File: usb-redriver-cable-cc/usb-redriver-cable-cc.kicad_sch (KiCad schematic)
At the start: 33 parts, among them J1 USB3 IN, J2 USB3 OUT, U1 PTN36241BBS, U2 SE8119AKN

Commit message: Transcribe strapping resistors with interpretations
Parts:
- R1, R10, R4, R7: value R -> 0
- R11, R13, R14, R2, R3, R5, R8, R9: value R -> DNP
- R12: value R -> 44k5
- R6: value R -> 38k
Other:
- note added: "Channel A & B Input signal threshold: 75 mV"
- note added: "Channel A Receive equalization: 7.5 dB Transmit de-emphasis: 0 dB Output swing: 1100 mV"
- note added: "Channel B Receive equalization: 7.5 dB Transmit de-emphasis: 0 dB Output swing: 1100 mV"
- moved on the sheet: C11, C12, C13, C14, C15, R1, R10, R2, R3, R4, R5, R6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

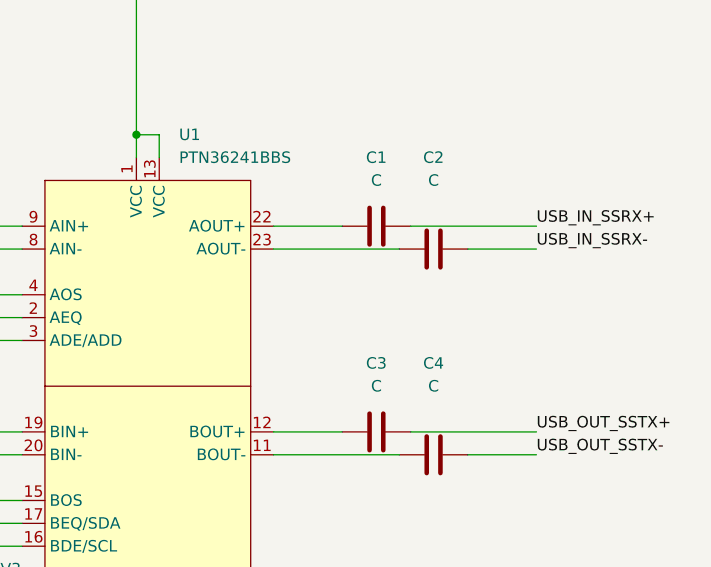
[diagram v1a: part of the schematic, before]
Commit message: Values for AC coupling capacitors
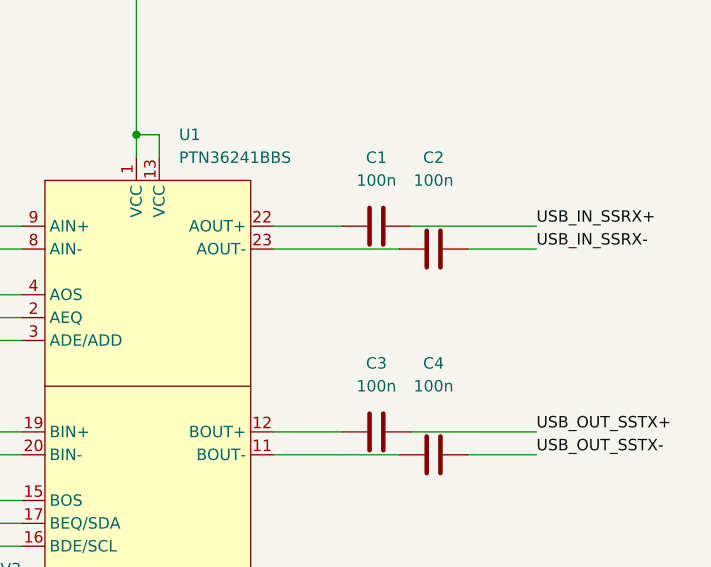
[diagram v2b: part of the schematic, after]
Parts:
- C1, C2, C3, C4: value C -> 100n
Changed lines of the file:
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@@
 			)
 		)
-		(property "Value" "C"
+		(property "Value" "100n"
 			(at 238.76 64.77 90)
 			(effects
@@
 			)
 		)
-		(property "Value" "C"
+		(property "Value" "100n"
 			(at 232.41 64.77 90)
 			(effects
@@
 			)
 		)
-		(property "Value" "C"
+		(property "Value" "100n"
 			(at 238.76 87.63 90)
 			(effects
@@
 			)
 		)
-		(property "Value" "C"
+		(property "Value" "100n"
 			(at 232.41 87.63 90)
 			(effects

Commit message: Footprint for AC coupling capacitors
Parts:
- C1, C2, C3, C4: footprint (none) -> Capacitor_SMD:C_0402_1005Metric
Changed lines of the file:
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@@
 			)
 		)
-		(property "Footprint" ""
+		(property "Footprint" "Capacitor_SMD:C_0402_1005Metric"
 			(at 242.57 71.4248 0)
 			(effects
@@
 			)
 		)
-		(property "Footprint" ""
+		(property "Footprint" "Capacitor_SMD:C_0402_1005Metric"
 			(at 236.22 68.8848 0)
 			(effects
@@
 			)
 		)
-		(property "Footprint" ""
+		(property "Footprint" "Capacitor_SMD:C_0402_1005Metric"
 			(at 242.57 94.2848 0)
 			(effects
@@
 			)
 		)
-		(property "Footprint" ""
+		(property "Footprint" "Capacitor_SMD:C_0402_1005Metric"
 			(at 236.22 91.7448 0)
 			(effects

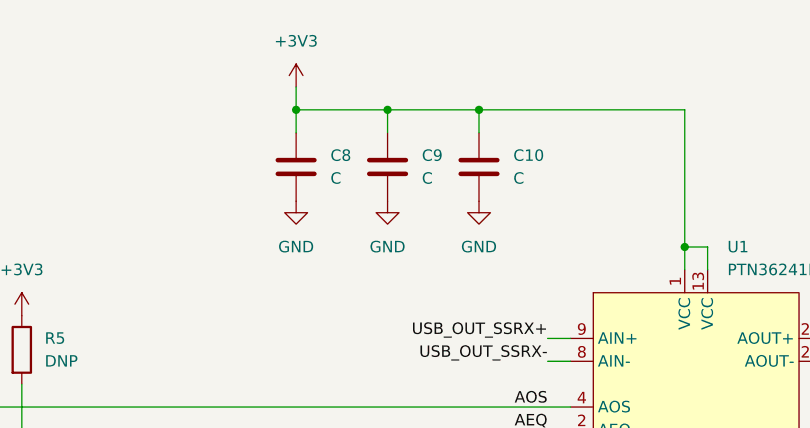
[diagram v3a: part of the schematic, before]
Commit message: Add values for redriver decoupling capacitors
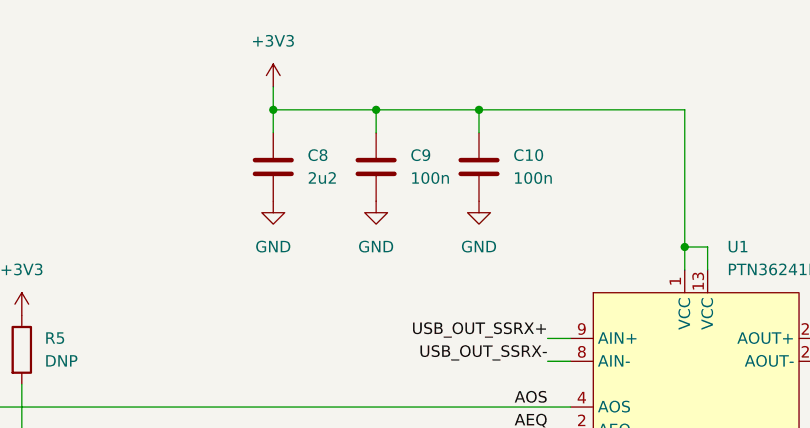
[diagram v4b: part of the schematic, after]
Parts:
- C10, C9: value C -> 100n; footprint (none) -> Capacitor_SMD:C_0402_1005Metric
- C8: value C -> 2u2; footprint (none) -> Capacitor_SMD:C_0805_2012Metric
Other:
- moved on the sheet: C8, C9
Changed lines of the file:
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@@
 	)
 	(junction
-		(at 162.56 44.45)
+		(at 160.02 44.45)
 		(diameter 0)
 		(color 0 0 0 0)
@@
 	)
 	(junction
-		(at 172.72 44.45)
+		(at 171.45 44.45)
 		(diameter 0)
 		(color 0 0 0 0)
@@
 	(wire
 		(pts
-			(xy 162.56 44.45) (xy 172.72 44.45)
+			(xy 160.02 44.45) (xy 171.45 44.45)
 		)
 		(stroke
@@
 	(wire
 		(pts
-			(xy 162.56 46.99) (xy 162.56 44.45)
+			(xy 160.02 46.99) (xy 160.02 44.45)
 		)
 		(stroke
@@
 	(wire
 		(pts
-			(xy 172.72 44.45) (xy 182.88 44.45)
+			(xy 171.45 44.45) (xy 182.88 44.45)
 		)
 		(stroke
@@
 	(wire
 		(pts
-			(xy 172.72 44.45) (xy 172.72 46.99)
+			(xy 171.45 44.45) (xy 171.45 46.99)
 		)
 		(stroke
@@
 	(wire
 		(pts
-			(xy 162.56 41.91) (xy 162.56 44.45)
+			(xy 160.02 41.91) (xy 160.02 44.45)
 		)
 		(stroke
@@
 	(symbol
 		(lib_id "Device:C")
-		(at 172.72 50.8 0)
+		(at 171.45 50.8 0)
 		(unit 1)
 		(exclude_from_sim no)
@@
 		(fields_autoplaced yes)
 		(property "Reference" "C9"
-			(at 176.53 49.5299 0)
+			(at 175.26 49.5299 0)
 			(effects
 				(font
@@
 			)
 		)
-		(property "Value" "C"
-			(at 176.53 52.0699 0)
+		(property "Value" "100n"
+			(at 175.26 52.0699 0)
 			(effects
 				(font
@@
 			)
 		)
-		(property "Footprint" ""
-			(at 173.6852 54.61 0)
+		(property "Footprint" "Capacitor_SMD:C_0402_1005Metric"
+			(at 172.4152 54.61 0)
 			(effects
 				(font
@@
 		)
 		(property "Datasheet" "~"
-			(at 172.72 50.8 0)
+			(at 171.45 50.8 0)
 			(effects
 				(font
@@
 		)
 		(property "Description" "Unpolarized capacitor"
-			(at 172.72 50.8 0)
+			(at 171.45 50.8 0)
 			(effects
 				(font
@@
 	(symbol
 		(lib_id "power:GND")
-		(at 162.56 54.61 0)
+		(at 160.02 54.61 0)
 		(unit 1)
 		(exclude_from_sim no)
@@
 		(fields_autoplaced yes)
 		(property "Reference" "#PWR024"
-			(at 162.56 60.96 0)
+			(at 160.02 60.96 0)
 			(effects
 				(font
@@
 		)
 		(property "Value" "GND"
-			(at 162.56 59.69 0)
+			(at 160.02 59.69 0)
 			(effects
 				(font
@@
 		)
 		(property "Footprint" ""
-			(at 162.56 54.61 0)
+			(at 160.02 54.61 0)
 			(effects
 				(font
@@
 		)
 		(property "Datasheet" ""
-			(at 162.56 54.61 0)
+			(at 160.02 54.61 0)
 			(effects
 				(font
@@
 		)
 		(property "Description" "Power symbol creates a global label with name \"GND\" , ground"
-			(at 162.56 54.61 0)
+			(at 160.02 54.61 0)
 			(effects
 				(font
@@
 	(symbol
 		(lib_id "power:+3V3")
-		(at 162.56 41.91 0)
+		(at 160.02 41.91 0)
 		(unit 1)
 		(exclude_from_sim no)
@@
 		(fields_autoplaced yes)
 		(property "Reference" "#PWR018"
-			(at 162.56 45.72 0)
+			(at 160.02 45.72 0)
 			(effects
 				(font
@@
 		)
 		(property "Value" "+3V3"
-			(at 162.56 36.83 0)
+			(at 160.02 36.83 0)
 			(effects
 				(font
@@
 		)
 		(property "Footprint" ""
-			(at 162.56 41.91 0)
+			(at 160.02 41.91 0)
 			(effects
 				(font
@@
 		)
 		(property "Datasheet" ""
-			(at 162.56 41.91 0)
+			(at 160.02 41.91 0)
 			(effects
 				(font
@@
 		)
 		(property "Description" "Power symbol creates a global label with name \"+3V3\""
-			(at 162.56 41.91 0)
+			(at 160.02 41.91 0)
 			(effects
 				(font
@@
 			)
 		)
-		(property "Value" "C"
+		(property "Value" "100n"
 			(at 186.69 52.0699 0)
 			(effects
@@
 			)
 		)
-		(property "Footprint" ""
+		(property "Footprint" "Capacitor_SMD:C_0402_1005Metric"
 			(at 183.8452 54.61 0)
 			(effects
@@
 	(symbol
 		(lib_id "power:GND")
-		(at 172.72 54.61 0)
+		(at 171.45 54.61 0)
 		(unit 1)
 		(exclude_from_sim no)
@@
 		(fields_autoplaced yes)
 		(property "Reference" "#PWR025"
-			(at 172.72 60.96 0)
+			(at 171.45 60.96 0)
 			(effects
 				(font
@@
 		)
 		(property "Value" "GND"
-			(at 172.72 59.69 0)
+			(at 171.45 59.69 0)
 			(effects
 				(font
@@
 		)
 		(property "Footprint" ""
-			(at 172.72 54.61 0)
+			(at 171.45 54.61 0)
 			(effects
 				(font
@@
 		)
 		(property "Datasheet" ""
-			(at 172.72 54.61 0)
+			(at 171.45 54.61 0)
 			(effects
 				(font
@@
 		)
 		(property "Description" "Power symbol creates a global label with name \"GND\" , ground"
-			(at 172.72 54.61 0)
+			(at 171.45 54.61 0)
 			(effects
 				(font
@@
 	(symbol
 		(lib_id "Device:C")
-		(at 162.56 50.8 0)
+		(at 160.02 50.8 0)
 		(unit 1)
 		(exclude_from_sim no)
@@
 		(fields_autoplaced yes)
 		(property "Reference" "C8"
-			(at 166.37 49.5299 0)
+			(at 163.83 49.5299 0)
 			(effects
 				(font
@@
 			)
 		)
-		(property "Value" "C"
-			(at 166.37 52.0699 0)
+		(property "Value" "2u2"
+			(at 163.83 52.0699 0)
 			(effects
 				(font
@@
 			)
 		)
-		(property "Footprint" ""
-			(at 163.5252 54.61 0)
+		(property "Footprint" "Capacitor_SMD:C_0805_2012Metric"
+			(at 160.9852 54.61 0)
 			(effects
 				(font
@@
 		)
 		(property "Datasheet" "~"
-			(at 162.56 50.8 0)
+			(at 160.02 50.8 0)
 			(effects
 				(font
@@
 		)
 		(property "Description" "Unpolarized capacitor"
-			(at 162.56 50.8 0)
+			(at 160.02 50.8 0)
 			(effects
 				(font

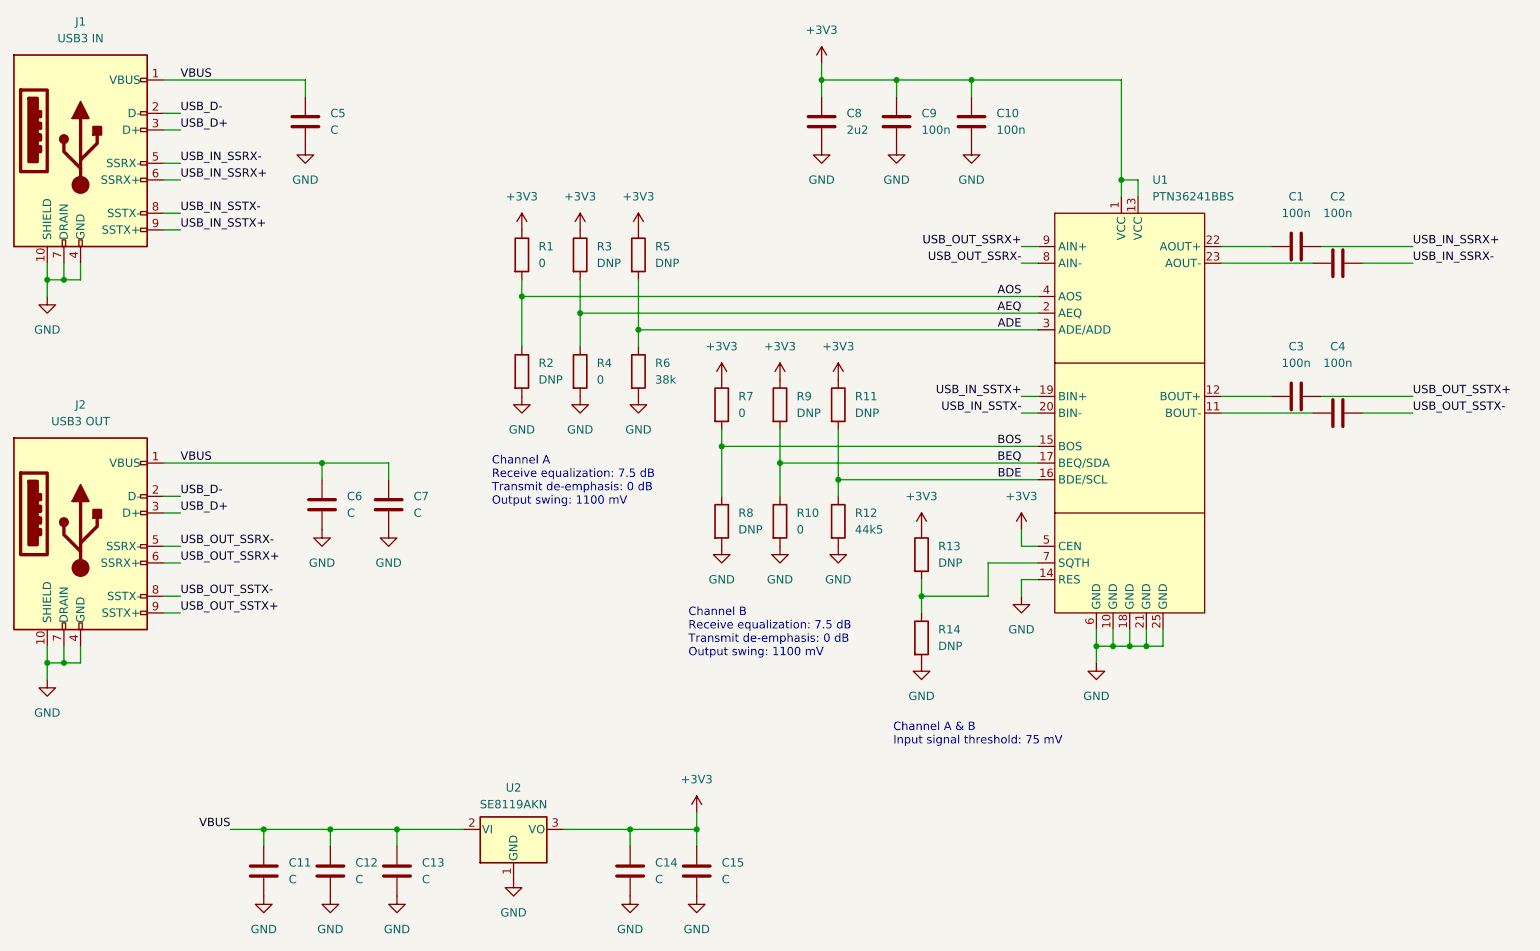
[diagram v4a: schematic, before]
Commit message: Add capacitance values for USB input and output
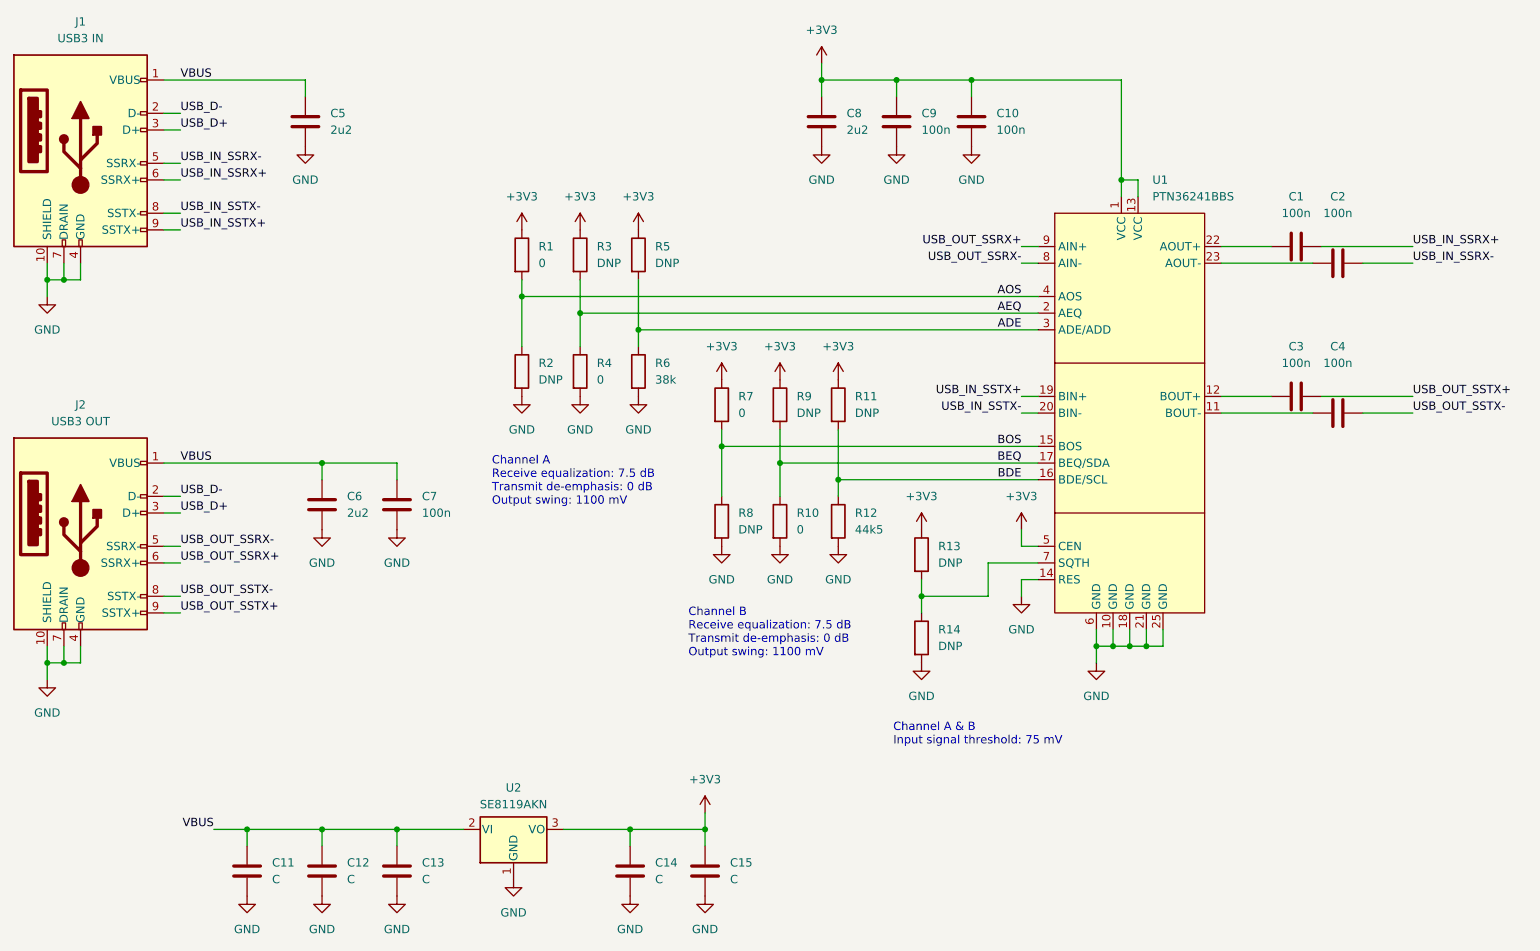
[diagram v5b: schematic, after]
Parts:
- C5, C6: value C -> 2u2; footprint (none) -> Capacitor_SMD:C_0805_2012Metric
- C7: value C -> 100n; footprint (none) -> Capacitor_SMD:C_0402_1005Metric
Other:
- moved on the sheet: C11, C12, C15, C7

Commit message: Add capacitance values for 3v3 regulator
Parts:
- C11, C14: value C -> 22u; footprint (none) -> Capacitor_SMD:C_1206_3216Metric
- C12, C13, C15: value C -> 100n; footprint (none) -> Capacitor_SMD:C_0402_1005Metric
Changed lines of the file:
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@@
 			)
 		)
-		(property "Value" "C"
+		(property "Value" "100n"
 			(at 99.06 166.3699 0)
 			(effects
@@
 			)
 		)
-		(property "Footprint" ""
+		(property "Footprint" "Capacitor_SMD:C_0402_1005Metric"
 			(at 96.2152 168.91 0)
 			(effects
@@
 			)
 		)
-		(property "Value" "C"
+		(property "Value" "100n"
 			(at 87.63 166.3699 0)
 			(effects
@@
 			)
 		)
-		(property "Footprint" ""
+		(property "Footprint" "Capacitor_SMD:C_0402_1005Metric"
 			(at 84.7852 168.91 0)
 			(effects
@@
 			)
 		)
-		(property "Value" "C"
+		(property "Value" "22u"
 			(at 76.2 166.3699 0)
 			(effects
@@
 			)
 		)
-		(property "Footprint" ""
+		(property "Footprint" "Capacitor_SMD:C_1206_3216Metric"
 			(at 73.3552 168.91 0)
 			(effects
@@
 			)
 		)
-		(property "Value" "C"
+		(property "Value" "22u"
 			(at 134.62 166.3699 0)
 			(effects
@@
 			)
 		)
-		(property "Footprint" ""
+		(property "Footprint" "Capacitor_SMD:C_1206_3216Metric"
 			(at 131.7752 168.91 0)
 			(effects
@@
 			)
 		)
-		(property "Value" "C"
+		(property "Value" "100n"
 			(at 146.05 166.3699 0)
 			(effects
@@
 			)
 		)
-		(property "Footprint" ""
+		(property "Footprint" "Capacitor_SMD:C_0402_1005Metric"
 			(at 143.2052 168.91 0)
 			(effects

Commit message: Add values for strapping resistors
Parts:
- R11, R13, R14, R2, R3, R5, R8, R9: now not fitted
- R12: value 44k5 -> 75k
- R6: value 38k -> 75k
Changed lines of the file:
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@@
 		(in_bom yes)
 		(on_board yes)
-		(dnp no)
+		(dnp yes)
 		(fields_autoplaced yes)
 		(property "Reference" "R3"
@@
 		(in_bom yes)
 		(on_board yes)
-		(dnp no)
+		(dnp yes)
 		(fields_autoplaced yes)
 		(property "Reference" "R11"
@@
 			)
 		)
-		(property "Value" "44k5"
+		(property "Value" "75k"
 			(at 165.1 113.0299 0)
 			(effects
@@
 		(in_bom yes)
 		(on_board yes)
-		(dnp no)
+		(dnp yes)
 		(fields_autoplaced yes)
 		(property "Reference" "R2"
@@
 		(in_bom yes)
 		(on_board yes)
-		(dnp no)
+		(dnp yes)
 		(fields_autoplaced yes)
 		(property "Reference" "R9"
@@
 		(in_bom yes)
 		(on_board yes)
-		(dnp no)
+		(dnp yes)
 		(fields_autoplaced yes)
 		(property "Reference" "R8"
@@
 		(in_bom yes)
 		(on_board yes)
-		(dnp no)
+		(dnp yes)
 		(fields_autoplaced yes)
 		(property "Reference" "R13"
@@
 		(in_bom yes)
 		(on_board yes)
-		(dnp no)
+		(dnp yes)
 		(fields_autoplaced yes)
 		(property "Reference" "R5"
@@
 			)
 		)
-		(property "Value" "38k"
+		(property "Value" "75k"
 			(at 134.62 90.1699 0)
 			(effects
@@
 		(in_bom yes)
 		(on_board yes)
-		(dnp no)
+		(dnp yes)
 		(fields_autoplaced yes)
 		(property "Reference" "R14"
